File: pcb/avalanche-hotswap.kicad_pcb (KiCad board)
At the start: 2 copper layers, 178.4 x 118.1 mm, 135 parts, among them J1 TRRS, J2 LED, J3 OLED, P1 i2c_pin, P2 i2c_pin, SW1 SW_Push, SW10 SW_Push, SW11 SW_Push, SW12 SW_Push, SW13 SW_Push, SW14 SW_Push, SW15 SW_Push, SW16 SW_Push, SW17 SW_Push, SW18 SW_Push, SW19 SW_Push, SW2 SW_Push, SW20 SW_Push, SW21 SW_Push, SW22 SW_Push, SW23 SW_Push, SW24 SW_Push, SW25 SW_Push, SW26 SW_Push, SW27 SW_Push, SW28 SW_Push, SW29 SW_Push, SW3 SW_Push, SW30 SW_Push, SW31 SW_Push, SW32 SW_Push, SW4 SW_Push, SW5 SW_Push, SW6 SW_Push, SW7 SW_Push, SW8 SW_Push, SW9 SW_Push, U1 ProMicro

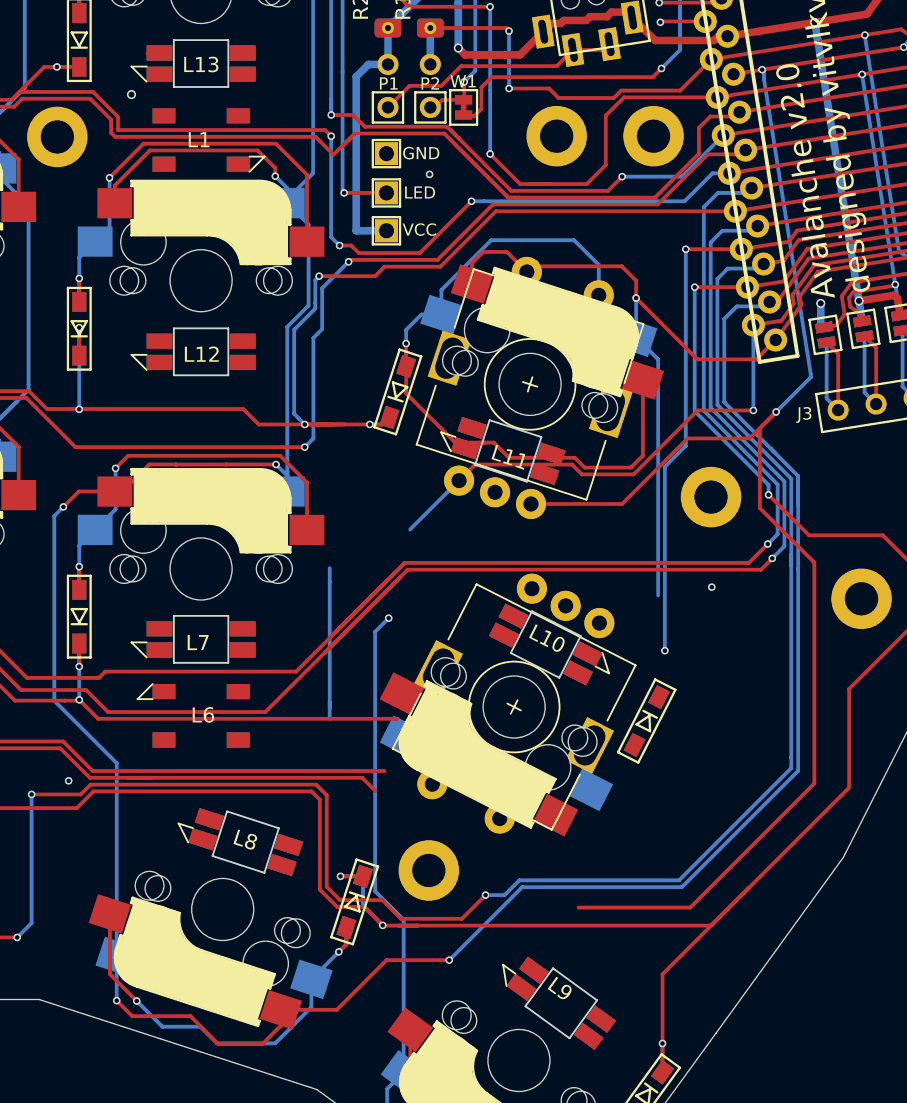
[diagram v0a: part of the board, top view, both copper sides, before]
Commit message: Routing encoder after rotate. Moved case hole a little.
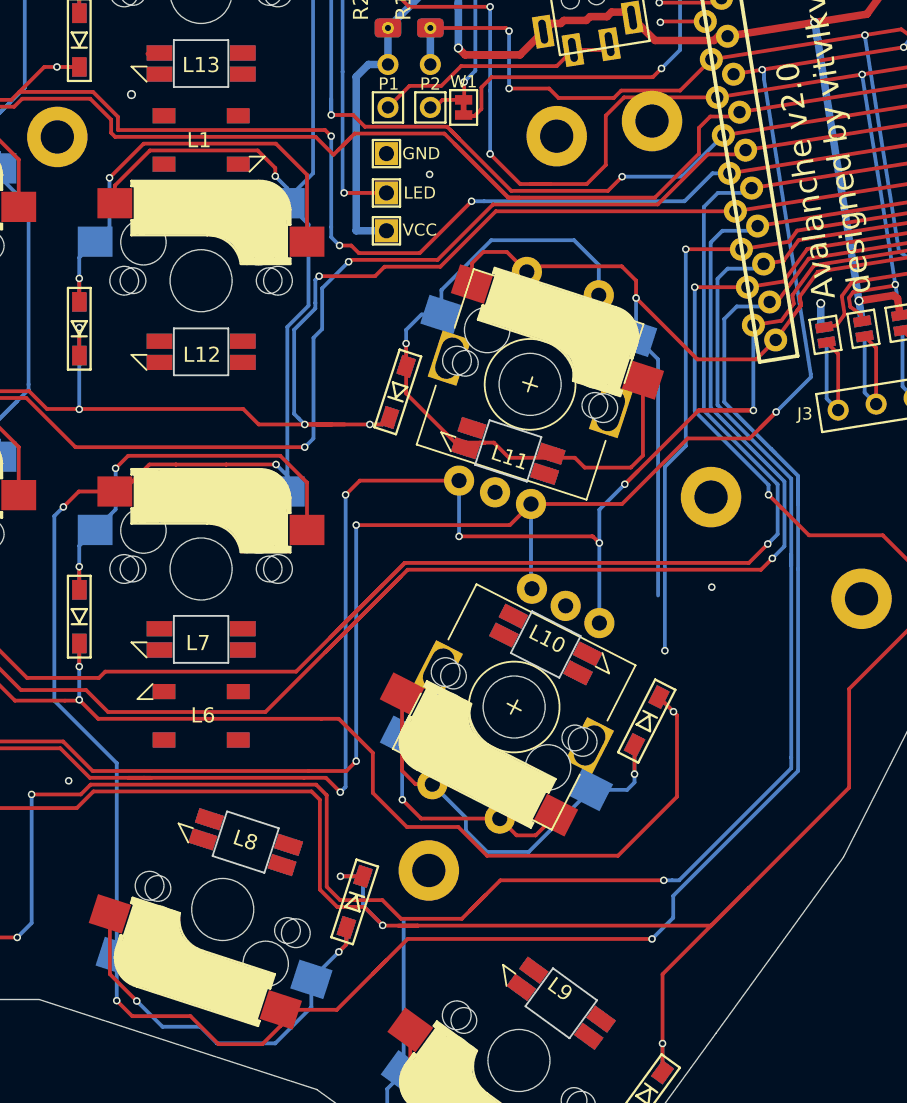
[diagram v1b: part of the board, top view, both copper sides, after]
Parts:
- moved H16 1.00 mm to (230.1, 73.8)
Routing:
- net encA: track 116.6 -> 154.0 mm, vias 1 -> 6
- net row3: track 217.5 -> 251.3 mm, vias 13 -> 14
- net sw27r: track 0.00 -> 29.5 mm, vias 0 -> 1
- net encB: track 172.3 -> 160.1 mm, vias 3 -> 5
- net ledA: track 10.4 -> 0.10 mm
- net col6: track 113.6 -> 108.3 mm
- net col5: track 274.2 -> 276.5 mm
- net col4: track 307.3 -> 308.7 mm

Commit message: WIP routing LEDs...
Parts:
- turned L1 to 180 degrees
- turned L2 to 180 degrees
- turned L3 to 180 degrees
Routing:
- net VCC: track 94.3 -> 478.9 mm, vias 3 -> 26
- net col0: track 313.1 -> 326.4 mm
- net row0: track 216.2 -> 211.0 mm, vias 9 -> 10
- net col3: track 344.1 -> 347.2 mm
- net Net-(D17-Pad2): track 27.7 -> 30.6 mm
- net row1: track 220.7 -> 220.0 mm
- net GND: vias 20 -> 17

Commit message: WIP routing LEDs...
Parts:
- turned L10 to 333 degrees
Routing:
- net VCC: track 478.9 -> 917.2 mm, vias 26 -> 51
- net sw20r: track 48.2 -> 34.9 mm, vias 1 -> 2
- net col6: track 108.3 -> 120.9 mm, vias 4 -> 5
- net col3: track 347.2 -> 339.5 mm, vias 9 -> 11
- net col2: track 280.5 -> 273.4 mm, vias 7 -> 9
- net row3: track 251.3 -> 254.5 mm, vias 14 -> 13
- net row2: track 252.8 -> 250.7 mm
- net row0: track 211.0 -> 209.0 mm
- net row4: track 330.2 -> 331.5 mm, vias 14 -> 13
- net col4: track 308.7 -> 308.1 mm
- net sw27r: track 29.5 -> 28.9 mm
- net GND: vias 17 -> 13

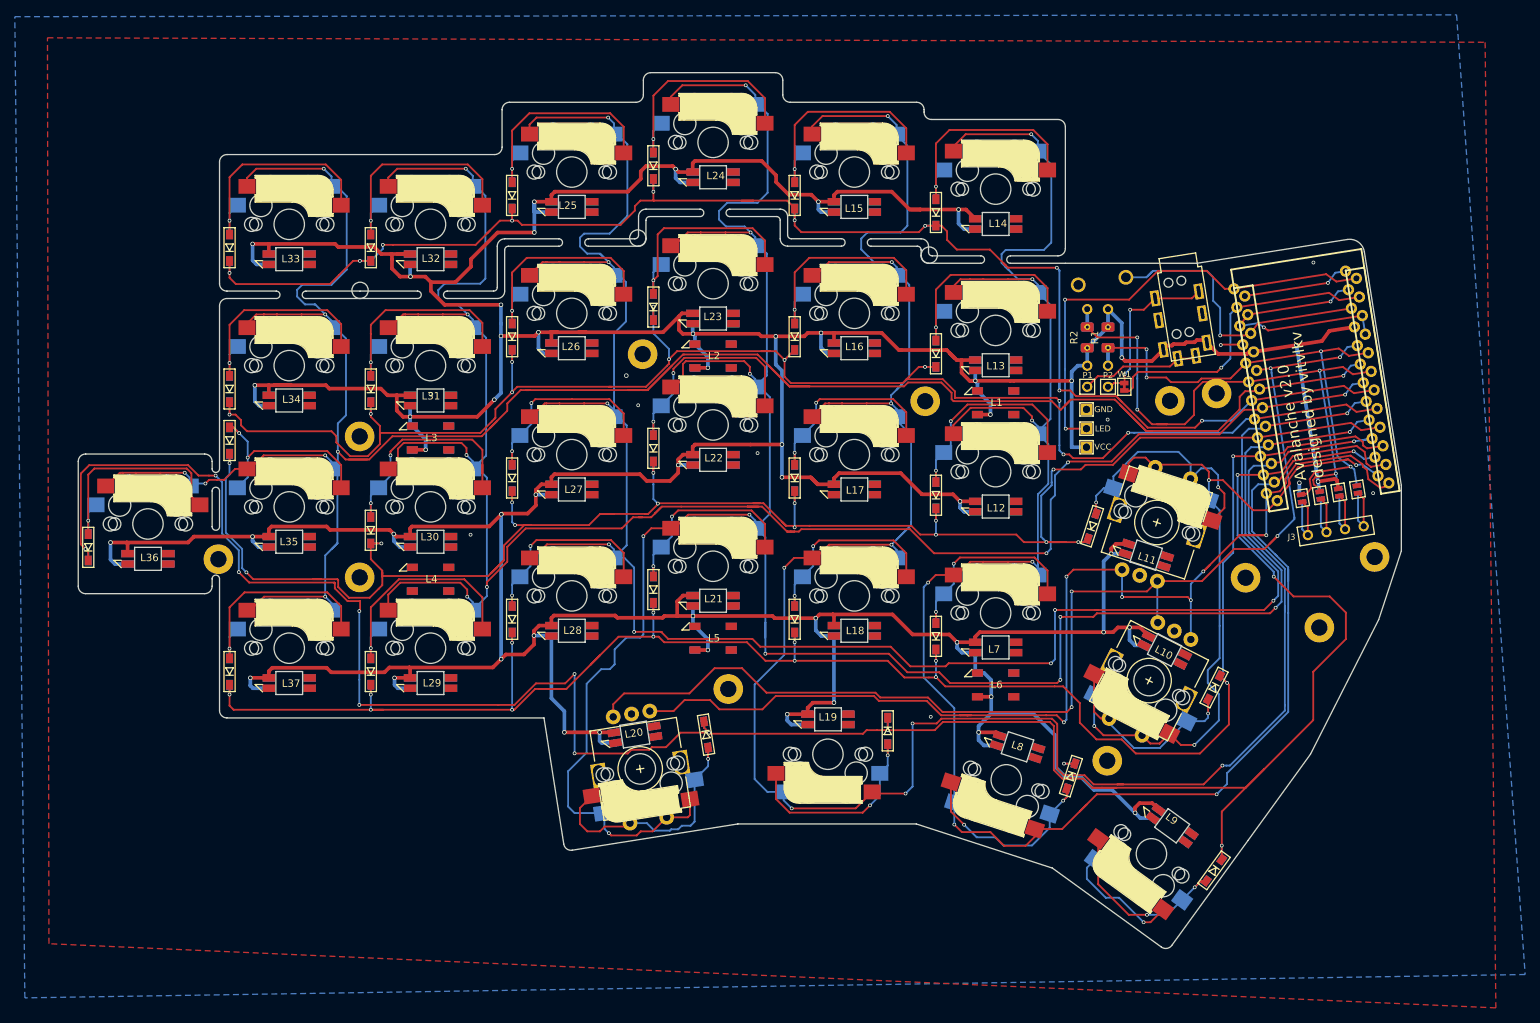
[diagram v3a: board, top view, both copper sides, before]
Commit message: WIP routing LEDs (done with "LED" track)
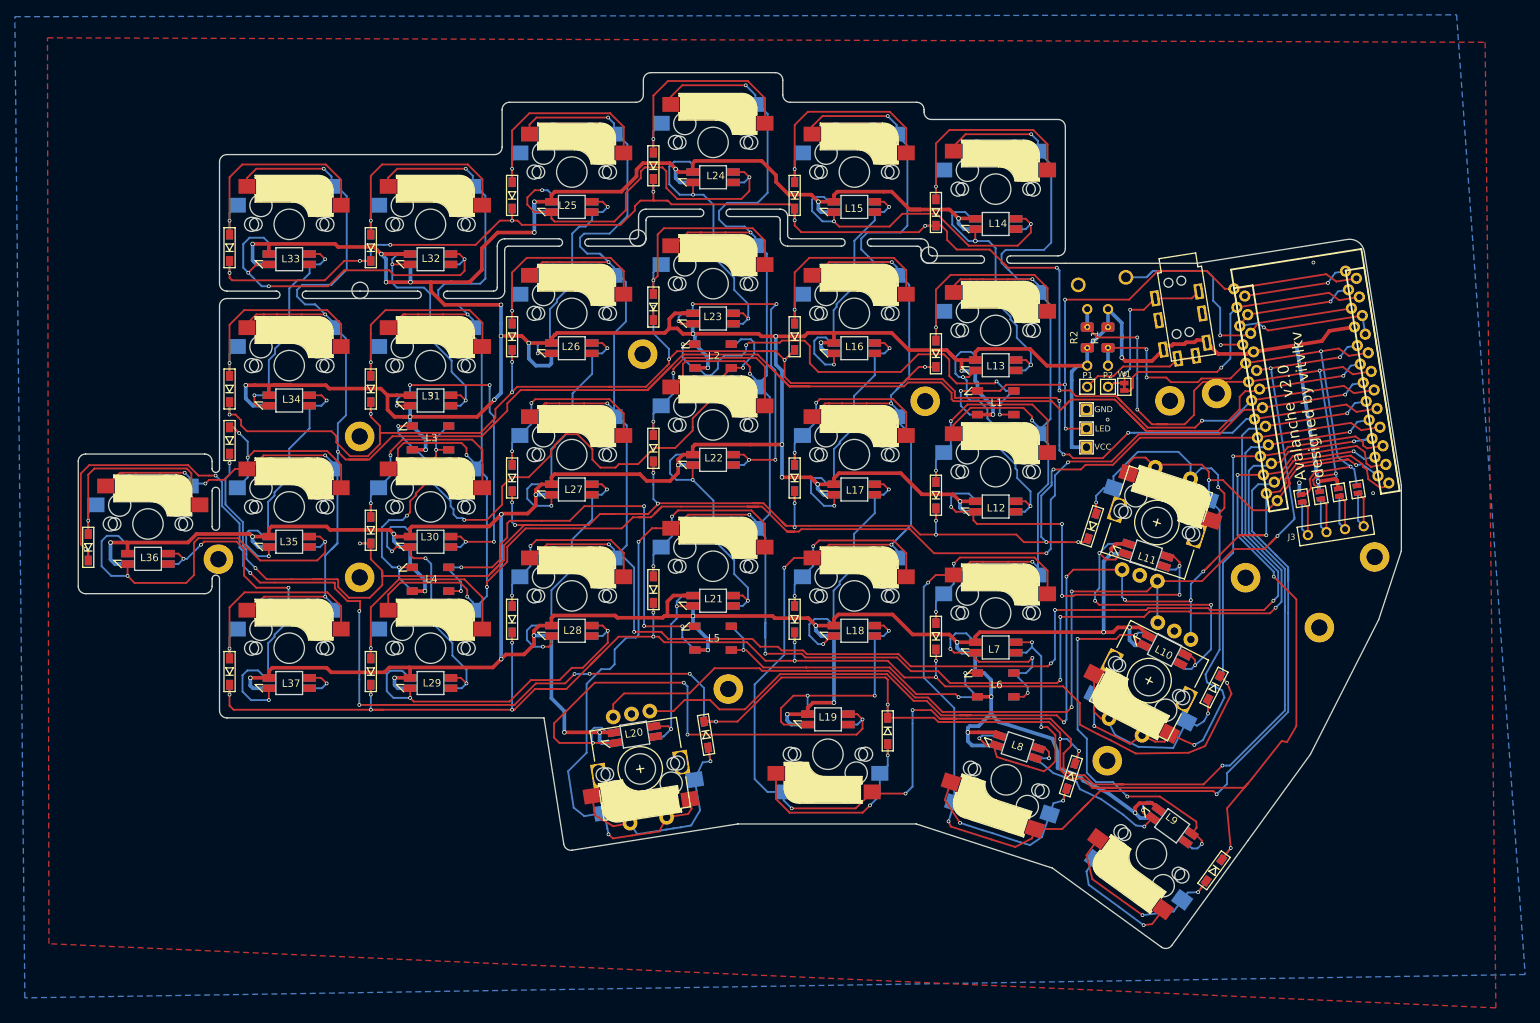
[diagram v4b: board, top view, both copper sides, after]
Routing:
- net Net-(L2-Pad1): track 0.00 -> 81.1 mm, vias 0 -> 3
- net Net-(L19-Pad1): track 0.00 -> 72.2 mm, vias 0 -> 4
- net Net-(L1-Pad1): track 0.00 -> 65.7 mm, vias 0 -> 4
- net Net-(L4-Pad1): track 0.90 -> 65.6 mm, vias 0 -> 5
- net Net-(L11-Pad1): track 0.00 -> 56.7 mm, vias 0 -> 5
- net Net-(L10-Pad3): track 0.00 -> 55.1 mm, vias 0 -> 4
- net Net-(L35-Pad1): track 0.00 -> 54.5 mm, vias 0 -> 2
- net Net-(L24-Pad1): track 0.00 -> 52.4 mm, vias 0 -> 2
- net Net-(L32-Pad1): track 0.00 -> 50.2 mm, vias 0 -> 3
- net ledD: track 0.00 -> 49.8 mm, vias 0 -> 4
- net Net-(L28-Pad1): track 0.00 -> 47.4 mm, vias 0 -> 2
- net Net-(L22-Pad1): track 0.00 -> 47.1 mm, vias 0 -> 5
- net Net-(L30-Pad1): track 0.00 -> 46.5 mm, vias 0 -> 5
- net Net-(L14-Pad1): track 0.00 -> 45.5 mm, vias 0 -> 2
- net Net-(L5-Pad1): track 2.00 -> 47.3 mm, vias 0 -> 3
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
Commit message: WIP routing the ground
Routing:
- net GND: track 44.8 -> 810.9 mm, vias 8 -> 71
- net col6: track 121.5 -> 144.8 mm
- net col5: track 276.7 -> 281.1 mm, vias 8 -> 10
- net LED: track 81.9 -> 86.4 mm
- net row2: track 249.8 -> 253.8 mm
- net encA: track 156.6 -> 153.6 mm
- net Net-(L35-Pad1): track 54.5 -> 57.2 mm
- net Net-(L32-Pad1): track 50.2 -> 52.0 mm
- net Net-(L7-Pad1): track 38.4 -> 36.7 mm
- net row4: track 321.8 -> 320.1 mm, vias 15 -> 13
- net Net-(L33-Pad1): track 30.2 -> 31.8 mm
- net col3: track 338.8 -> 337.4 mm
- net VCC: track 946.6 -> 947.9 mm, vias 54 -> 57
- net col0: track 326.4 -> 327.6 mm
- net Net-(L10-Pad3): track 55.1 -> 56.2 mm
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
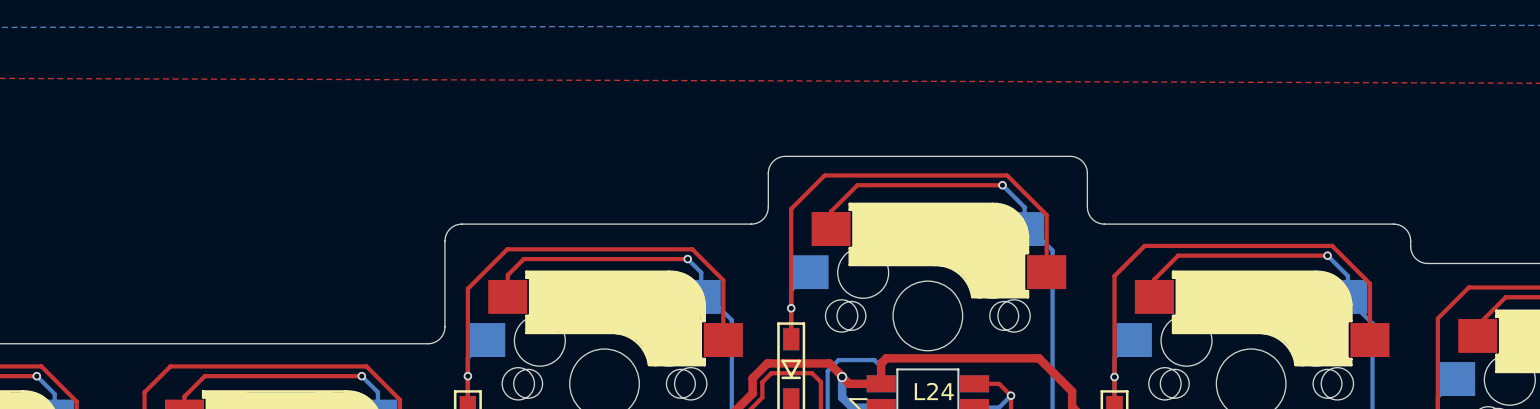
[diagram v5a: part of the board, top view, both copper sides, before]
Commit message: Added jumpers for LEDs in case of nums row break-off
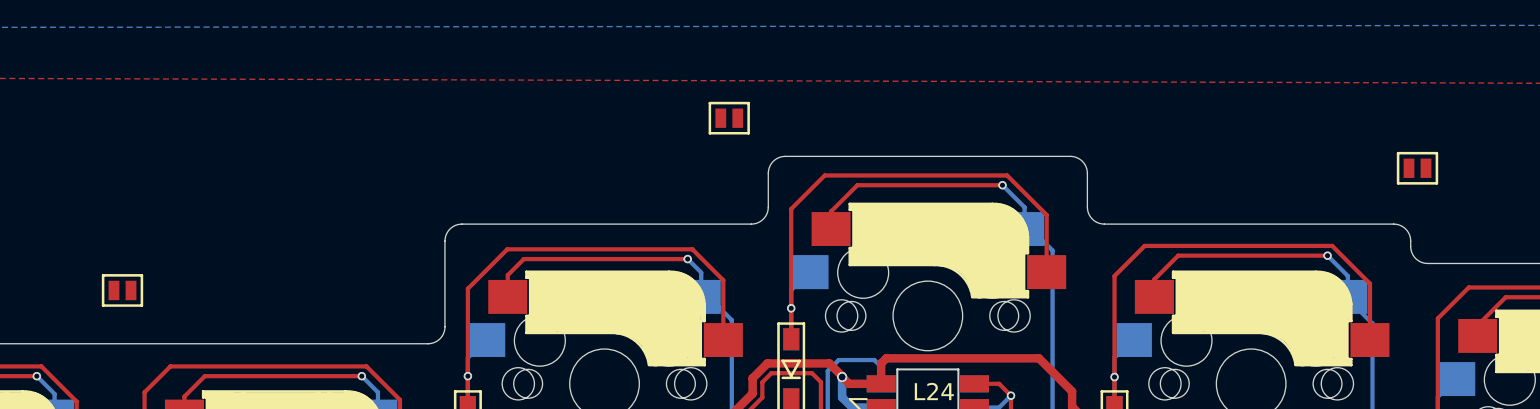
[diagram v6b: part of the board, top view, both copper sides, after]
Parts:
- added JP10: Device_Jumper_NO_Small, used_footprints:avalanche_Jumper, F.Cu at (150.4, 28.3)
- added JP11: Device_Jumper_NO_Small, used_footprints:avalanche_Jumper, F.Cu at (114.7, 38.5)
- added JP9: Device_Jumper_NO_Small, used_footprints:avalanche_Jumper, F.Cu at (191.0, 31.2)
- L31: value e -> SK6812MINI_LED

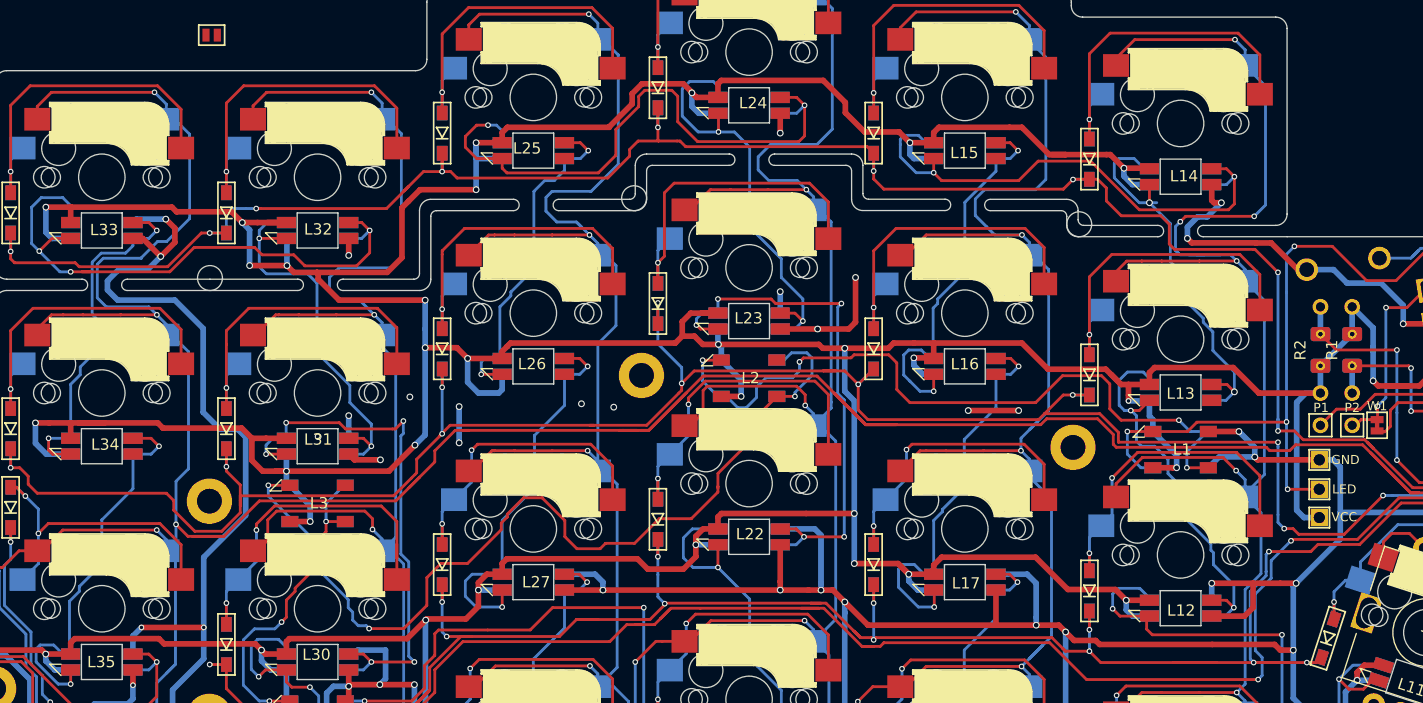
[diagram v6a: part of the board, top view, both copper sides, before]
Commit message: Routed the ground
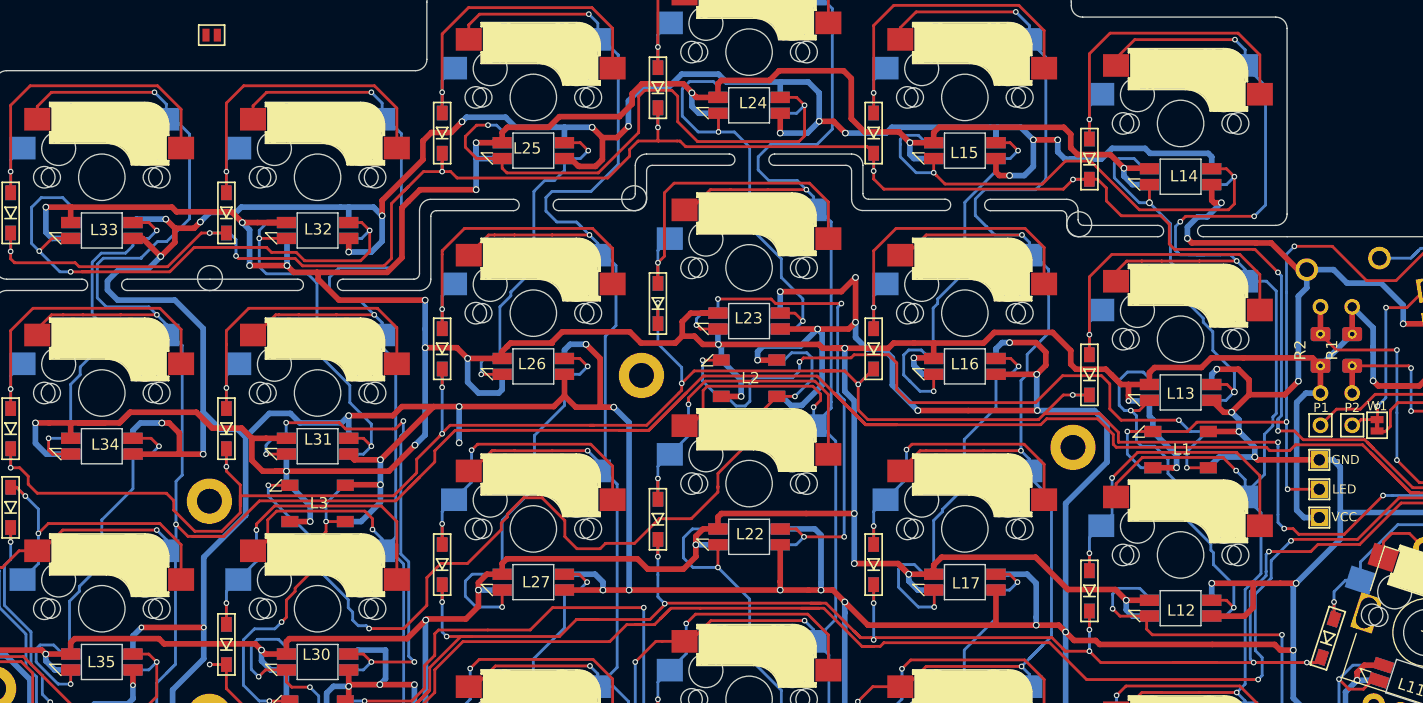
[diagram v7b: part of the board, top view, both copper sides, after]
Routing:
- net GND: track 810.9 -> 1159.1 mm, vias 71 -> 90
- net VCC: track 947.9 -> 955.0 mm
- net row0: track 207.4 -> 212.8 mm
- net col5: track 281.1 -> 283.1 mm
- net col3: track 337.4 -> 338.8 mm
- net col4: track 311.8 -> 310.8 mm
- net Net-(JP9-Pad2): track 35.6 -> 34.9 mm
